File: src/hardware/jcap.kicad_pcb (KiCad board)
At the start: 2 copper layers, 136.8 x 87 mm, 66 parts, among them J201 CPU PGMR, J202 SPARE CPU HDR, J203 GPU PGMR, J204 SPARE GPU HDR, J301 DC IN, J501 VGA OUT, J601 CONTROLS, Q301 IPP80P03P4L-04, SW201 CPU ~{RES}, SW202 DEBUG, SW203 GPU ~{RES}, SW601 TILT, U201 P8X32A, U202 P8X32A, U301 LM3940IT, U401 24LC256, U402 24LC256, U601 74HC165, U602 74HC165, Y201 6.5MHz, Y202 6.5MHz

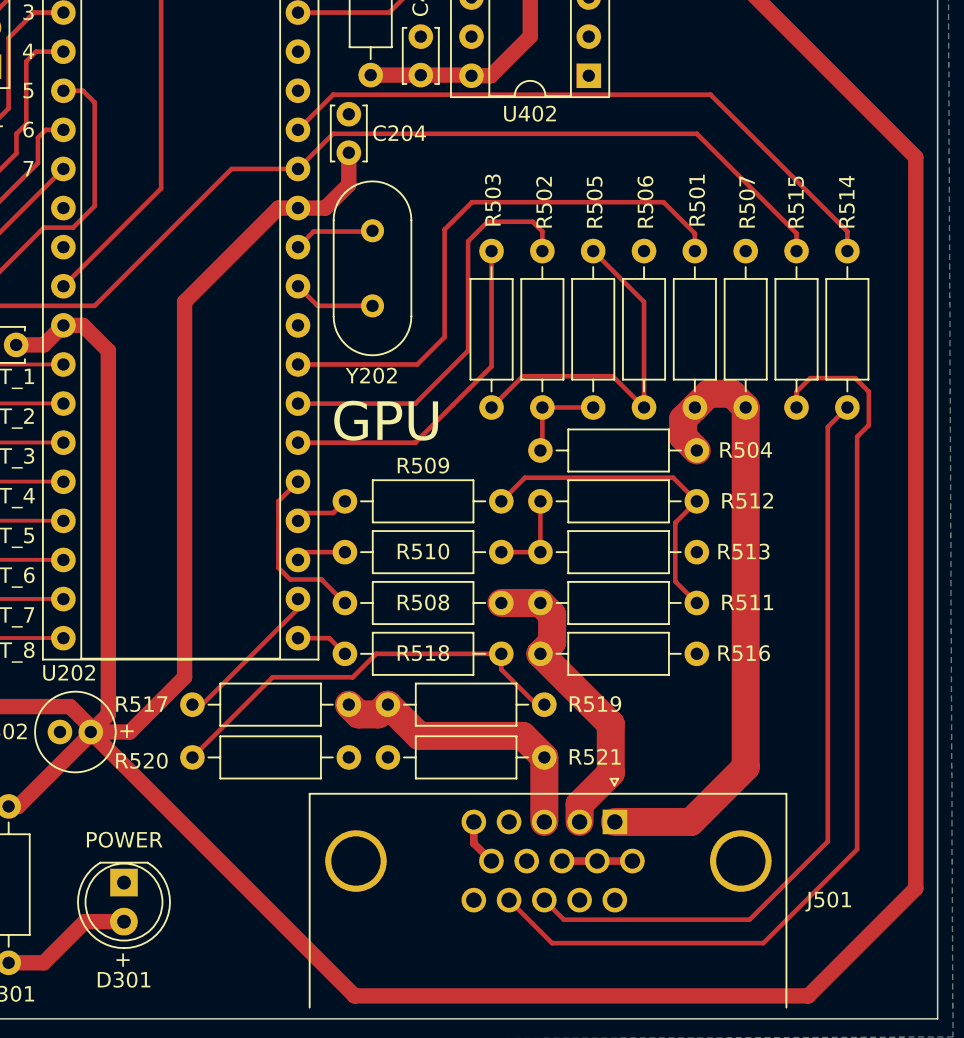
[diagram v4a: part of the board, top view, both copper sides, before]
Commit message: Swapped H/VSync pins
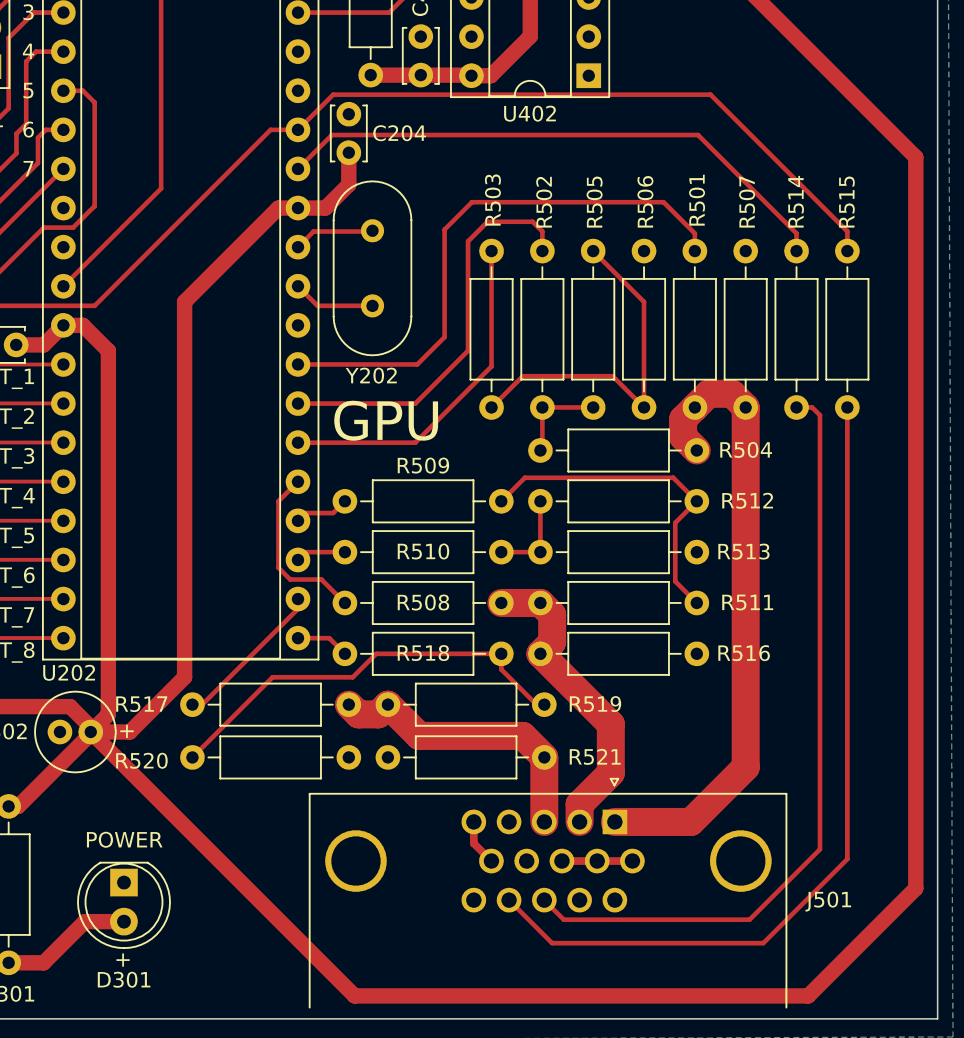
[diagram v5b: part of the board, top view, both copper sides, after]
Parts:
- moved R514 3.30 mm to (205.4, 88.5)
- moved R515 3.30 mm to (208.7, 88.5)
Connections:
- U202 pad 33: V_SYNC -> H_SYNC
- U202 pad 34: H_SYNC -> V_SYNC
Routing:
- net Net-(J501-Pad14): track 62.8 -> 54.7 mm
- net V_SYNC: track 106.3 -> 111.8 mm
- net H_SYNC: track 41.6 -> 37.1 mm
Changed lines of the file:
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@@
       (net 1 "+3.3V") (pinfunction "VDD") (pintype "power_in"))
     (pad "33" thru_hole oval (at 15.24 17.78) (size 1.6 1.6) (drill 0.8) (layers "*.Cu" "*.Mask")
-      (net 44 "V_SYNC") (pinfunction "P24") (pintype "bidirectional"))
+      (net 43 "H_SYNC") (pinfunction "P24") (pintype "bidirectional"))
     (pad "34" thru_hole oval (at 15.24 15.24) (size 1.6 1.6) (drill 0.8) (layers "*.Cu" "*.Mask")
-      (net 43 "H_SYNC") (pinfunction "P25") (pintype "bidirectional"))
+      (net 44 "V_SYNC") (pinfunction "P25") (pintype "bidirectional"))
     (pad "35" thru_hole oval (at 15.24 12.7) (size 1.6 1.6) (drill 0.8) (layers "*.Cu" "*.Mask")
       (net 98 "unconnected-(U202-P26-Pad35)") (pinfunction "P26") (pintype "bidirectional+no_connect"))
@@
   )
   (footprint "Resistor_THT:R_Axial_DIN0207_L6.3mm_D2.5mm_P10.16mm_Horizontal" (layer "F.Cu")
-    (at 205.359 88.519 -90)
+    (at 208.661 88.519 -90)
     (descr "Resistor, Axial_DIN0207 series, Axial, Horizontal, pin pitch=10.16mm, 0.25W = 1/4W, length*diameter=6.3*2.5mm^2, http://cdn-reichelt.de/documents/datenblatt/B400/1_4W%23YAG.pdf")
     (tags "Resistor Axial_DIN0207 series Axial Horizontal pin pitch 10.16mm 0.25W = 1/4W length 6.3mm diameter 2.5mm")
@@
   )
   (footprint "Resistor_THT:R_Axial_DIN0207_L6.3mm_D2.5mm_P10.16mm_Horizontal" (layer "F.Cu")
-    (at 208.661 88.519 -90)
+    (at 205.359 88.519 -90)
     (descr "Resistor, Axial_DIN0207 series, Axial, Horizontal, pin pitch=10.16mm, 0.25W = 1/4W, length*diameter=6.3*2.5mm^2, http://cdn-reichelt.de/documents/datenblatt/B400/1_4W%23YAG.pdf")
     (tags "Resistor Axial_DIN0207 series Axial Horizontal pin pitch 10.16mm 0.25W = 1/4W length 6.3mm diameter 2.5mm")
@@
   (segment (start 172.974 113.665) (end 175.006 113.665) (width 0.3) (layer "F.Cu") (net 42))
   (segment (start 175.006 113.665) (end 176.022 114.681) (width 0.3) (layer "F.Cu") (net 42))
-  (segment (start 175.26 78.359) (end 172.974 80.645) (width 0.3) (layer "F.Cu") (net 43))
-  (segment (start 208.661 87.249) (end 199.771 78.359) (width 0.3) (layer "F.Cu") (net 43))
-  (segment (start 199.771 78.359) (end 175.26 78.359) (width 0.3) (layer "F.Cu") (net 43))
-  (segment (start 208.661 88.519) (end 208.661 87.249) (width 0.3) (layer "F.Cu") (net 43))
-  (segment (start 140.97 90.805) (end 142.24 92.075) (width 0.3) (layer "F.Cu") (net 44))
+  (segment (start 175.18 80.979) (end 198.962 80.979) (width 0.3) (layer "F.Cu") (net 43))
+  (segment (start 198.962 80.979) (end 205.359 87.376) (width 0.3) (layer "F.Cu") (net 43))
+  (segment (start 172.974 83.185) (end 175.18 80.979) (width 0.3) (layer "F.Cu") (net 43))
+  (segment (start 205.359 87.376) (end 205.359 88.519) (width 0.3) (layer "F.Cu") (net 43))
   (segment (start 142.24 92.075) (end 159.766 92.075) (width 0.3) (layer "F.Cu") (net 44))
-  (segment (start 133.853 78.095) (end 138.669 73.279) (width 0.3) (layer "F.Cu") (net 44))
-  (segment (start 198.882 80.899) (end 175.26 80.899) (width 0.3) (layer "F.Cu") (net 44))
-  (segment (start 138.669 73.279) (end 142.748 73.279) (width 0.3) (layer "F.Cu") (net 44))
-  (segment (start 205.359 87.376) (end 198.882 80.899) (width 0.3) (layer "F.Cu") (net 44))
+  (segment (start 140.97 82.677) (end 140.97 90.805) (width 0.3) (layer "F.Cu") (net 44))
+  (segment (start 175.26 78.359) (end 199.771 78.359) (width 0.3) (layer "F.Cu") (net 44))
+  (segment (start 172.974 80.645) (end 175.26 78.359) (width 0.3) (layer "F.Cu") (net 44))
+  (segment (start 144.78 75.311) (end 145.923 75.311) (width 0.3) (layer "F.Cu") (net 44))
   (segment (start 146.558 77.089) (end 140.97 82.677) (width 0.3) (layer "F.Cu") (net 44))
-  (segment (start 159.766 92.075) (end 168.656 83.185) (width 0.3) (layer "F.Cu") (net 44))
+  (segment (start 199.771 78.359) (end 208.661 87.249) (width 0.3) (layer "F.Cu") (net 44))
   (segment (start 142.748 73.279) (end 144.78 75.311) (width 0.3) (layer "F.Cu") (net 44))
-  (segment (start 205.359 88.519) (end 205.359 87.376) (width 0.3) (layer "F.Cu") (net 44))
-  (segment (start 144.78 75.311) (end 145.923 75.311) (width 0.3) (layer "F.Cu") (net 44))
-  (segment (start 175.26 80.899) (end 172.974 83.185) (width 0.3) (layer "F.Cu") (net 44))
+  (segment (start 138.669 73.279) (end 142.748 73.279) (width 0.3) (layer "F.Cu") (net 44))
+  (segment (start 208.661 87.249) (end 208.661 88.519) (width 0.3) (layer "F.Cu") (net 44))
+  (segment (start 159.766 92.075) (end 171.196 80.645) (width 0.3) (layer "F.Cu") (net 44))
+  (segment (start 133.853 78.095) (end 138.669 73.279) (width 0.3) (layer "F.Cu") (net 44))
+  (segment (start 171.196 80.645) (end 172.974 80.645) (width 0.3) (layer "F.Cu") (net 44))
   (segment (start 146.558 75.946) (end 146.558 77.089) (width 0.3) (layer "F.Cu") (net 44))
+  (segment (start 140.97 90.805) (end 142.24 92.075) (width 0.3) (layer "F.Cu") (net 44))
   (segment (start 145.923 75.311) (end 146.558 75.946) (width 0.3) (layer "F.Cu") (net 44))
-  (segment (start 140.97 82.677) (end 140.97 90.805) (width 0.3) (layer "F.Cu") (net 44))
-  (segment (start 168.656 83.185) (end 172.974 83.185) (width 0.3) (layer "F.Cu") (net 44))
   (segment (start 83.566 90.551) (end 85.471 88.646) (width 0.3) (layer "F.Cu") (net 45))
   (segment (start 85.471 83.566) (end 87.376 81.661) (width 0.3) (layer "F.Cu") (net 45))
@@
   (segment (start 148.6635 57.023) (end 150.4415 55.245) (width 0.3) (layer "F.Cu") (net 82))
   (segment (start 170.434 55.245) (end 173.482 58.293) (width 0.3) (layer "F.Cu") (net 82))
-  (segment (start 207.391 126.873) (end 202.311 131.953) (width 0.3) (layer "F.Cu") (net 87))
-  (segment (start 190.246 131.953) (end 188.976 130.683) (width 0.3) (layer "F.Cu") (net 87))
-  (segment (start 208.661 98.679) (end 207.391 99.949) (width 0.3) (layer "F.Cu") (net 87))
-  (segment (start 207.391 99.949) (end 207.391 126.873) (width 0.3) (layer "F.Cu") (net 87))
   (segment (start 202.311 131.953) (end 190.246 131.953) (width 0.3) (layer "F.Cu") (net 87))
-  (segment (start 189.48 133.477) (end 186.686 130.683) (width 0.3) (layer "F.Cu") (net 88))
-  (segment (start 210.058 97.663) (end 210.058 99.822) (width 0.3) (layer "F.Cu") (net 88))
-  (segment (start 209.169 96.774) (end 210.058 97.663) (width 0.3) (layer "F.Cu") (net 88))
-  (segment (start 205.359 97.663) (end 206.248 96.774) (width 0.3) (layer "F.Cu") (net 88))
-  (segment (start 205.359 98.679) (end 205.359 97.663) (width 0.3) (layer "F.Cu") (net 88))
-  (segment (start 209.296 127.381) (end 203.2 133.477) (width 0.3) (layer "F.Cu") (net 88))
+  (segment (start 190.246 131.953) (end 188.976 130.683) (width 0.3) (layer "F.Cu") (net 87))
+  (segment (start 206.883 127.381) (end 202.311 131.953) (width 0.3) (layer "F.Cu") (net 87))
+  (segment (start 205.359 98.679) (end 206.375 98.679) (width 0.3) (layer "F.Cu") (net 87))
+  (segment (start 206.883 99.187) (end 206.883 127.381) (width 0.3) (layer "F.Cu") (net 87))
+  (segment (start 206.375 98.679) (end 206.883 99.187) (width 0.3) (layer "F.Cu") (net 87))
+  (segment (start 208.661 128.016) (end 203.2 133.477) (width 0.3) (layer "F.Cu") (net 88))
   (segment (start 203.2 133.477) (end 189.48 133.477) (width 0.3) (layer "F.Cu") (net 88))
-  (segment (start 210.058 99.822) (end 209.296 100.584) (width 0.3) (layer "F.Cu") (net 88))
-  (segment (start 209.296 100.584) (end 209.296 127.381) (width 0.3) (layer "F.Cu") (net 88))
-  (segment (start 206.248 96.774) (end 209.169 96.774) (width 0.3) (layer "F.Cu") (net 88))
+  (segment (start 208.661 98.679) (end 208.661 128.016) (width 0.3) (layer "F.Cu") (net 88))
+  (segment (start 189.48 133.477) (end 186.686 130.683) (width 0.3) (layer "F.Cu") (net 88))
   (segment (start 188.849 98.679) (end 188.849 101.346) (width 0.3) (layer "F.Cu") (net 90))
   (segment (start 188.849 98.679) (end 192.151 98.679) (width 0.3) (layer "F.Cu") (net 90))
